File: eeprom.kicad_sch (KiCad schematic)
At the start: 4 parts, among them U2 AT24C04C_SOIC8

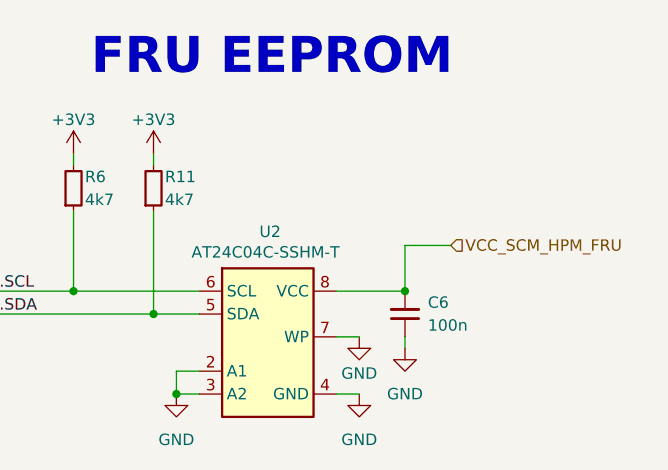
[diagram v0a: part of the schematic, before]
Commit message: [#92504] Add LTPI connector
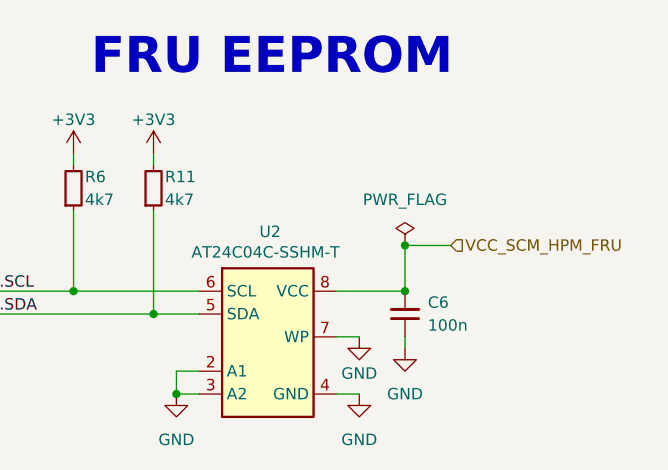
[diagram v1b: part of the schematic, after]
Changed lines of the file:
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@@
+	)
+	(junction
+		(at 100.33 45.72)
+		(diameter 0)
+		(color 0 0 0 0)
 	)
 	(junction
@@
 					(unit 1)
 				)
+			)
+		)
+	)
+	(symbol
+		(lib_name "PWR_FLAG_1")
+		(lib_id "antmicropower:PWR_FLAG")
+		(at 100.33 45.72 0)
+		(unit 1)
+		(exclude_from_sim no)
+		(in_bom yes)
+		(on_board yes)
+		(dnp no)
+		(fields_autoplaced yes)
+		(property "Reference" "#FLG04"
+			(at 100.33 43.815 0)
+			(effects
+				(font
+					(size 1.27 1.27)
+				)
+				(hide yes)
+			)
+		)
+		(property "Value" "PWR_FLAG"
+			(at 100.33 40.64 0)
+			(effects
+				(font
+					(size 1.27 1.27)
+				)
+			)
+		)
+		(property "Footprint" ""
+			(at 100.33 45.72 0)
+			(effects
+				(font
+					(size 1.27 1.27)
+				)
+				(hide yes)
+			)
+		)
+		(property "Datasheet" ""
+			(at 100.33 45.72 0)
+			(effects
+				(font
+					(size 1.27 1.27)
+				)
+				(hide yes)
+			)
+		)
+		(property "Description" ""
+			(at 100.33 48.26 0)
+			(effects
+				(font
+					(size 1.27 1.27)
+				)
+				(justify left bottom)
+				(hide yes)
+			)
+		)
+		(pin "1"
+		)
+		(instances
+			(project "bmc-breakout-board"
+				(path "/5d67ef28-5805-4f87-b722-2926dabf7f6e/2af4bc97-3599-45a7-a55a-50109ab85386"
+					(reference "#FLG04")
+					(unit 1)
+				)

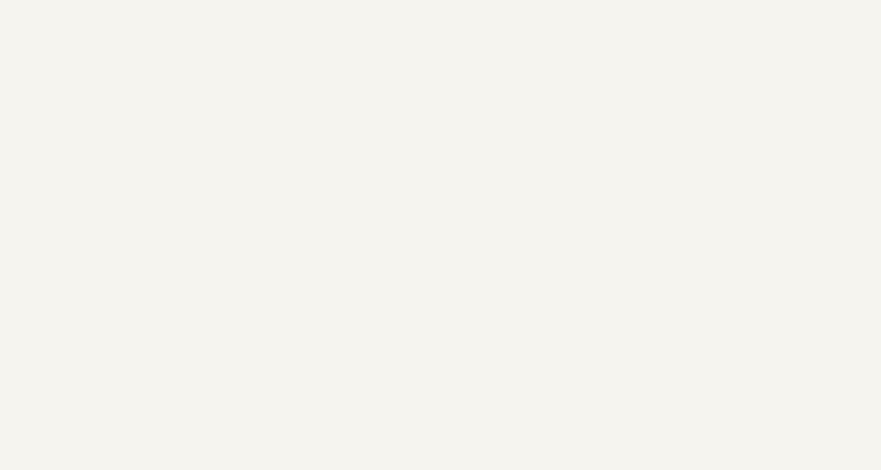
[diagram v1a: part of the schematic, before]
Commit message: [#92504] Add EEPROM power LED + TP
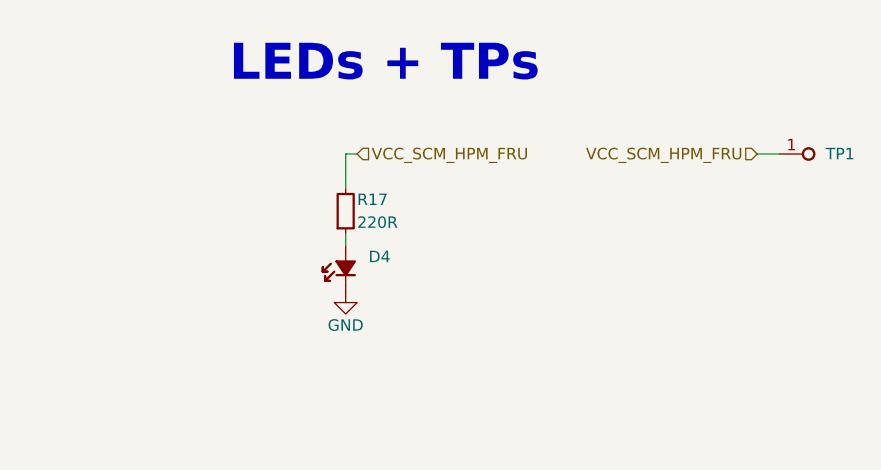
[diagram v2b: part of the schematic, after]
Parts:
- added D4: LED_G_0402_VLMTG1500-GS08, antmicro-footprints:LED_0402_1005Metric_G, symbol antmicroLEDIndicationDiscrete:LED_G_0402_VLMTG1500-GS08
- added R17: R_220R_0402, antmicro-footprints:R_0402_1005Metric, symbol antmicroResistors0402:R_220R_0402
- added TP1: TP_0.75mm_SMD, antmicro-footprints:TP_SMD_0.75mm, symbol antmicroTestPoints:TP_0.75mm_SMD
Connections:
- net GND: now also D4.1 (C)
- net VCC_SCM_HPM_FRU: now also R17.2, TP1.1
- new net: D4.2 (A), R17.1
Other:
- note added: "LEDs + TPs"

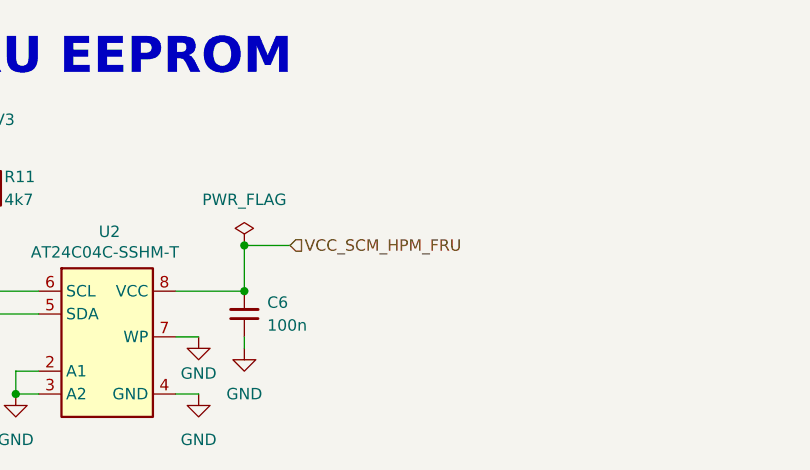
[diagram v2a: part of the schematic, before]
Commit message: [#92504] Add pull-up resistors for QWIIC
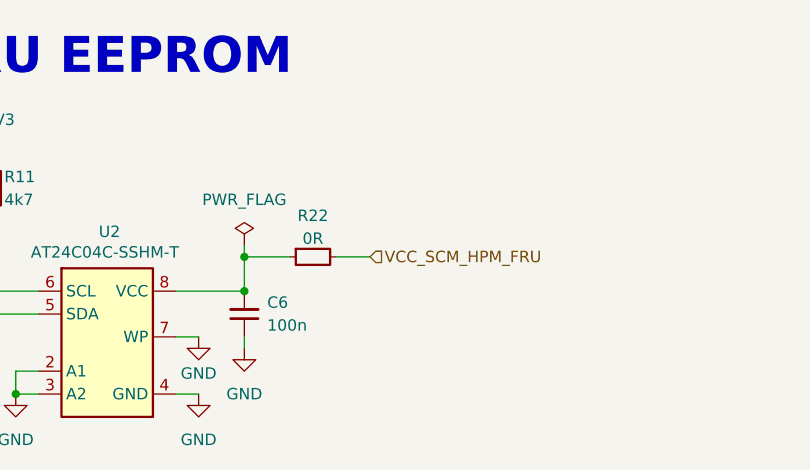
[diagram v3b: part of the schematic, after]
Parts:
- added R22: R_0R_0402, antmicro-footprints:R_0402_1005Metric, symbol antmicroResistors0402:R_0R_0402
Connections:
- net VCC_SCM_HPM_FRU: now also R22.2; no longer C6.2, U2.8 (VCC)
- new net: C6.2, R22.1, U2.8 (VCC)
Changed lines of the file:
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@@
-	)
-	(junction
-		(at 100.33 45.72)
-		(diameter 0)
-		(color 0 0 0 0)
 	)
 	(junction
@@
 	)
 	(junction
+		(at 100.33 46.99)
+		(diameter 0)
+		(color 0 0 0 0)
+	)
+	(junction
 		(at 72.39 53.34)
 		(diameter 0)
@@
 	(wire
 		(pts
+			(xy 110.49 46.99) (xy 114.3 46.99)
+		)
+		(stroke
+			(width 0)
+			(type default)
+		)
+	)
+	(wire
+		(pts
 			(xy 92.71 55.88) (xy 95.25 55.88)
 		)
@@
 	(wire
 		(pts
+			(xy 100.33 46.99) (xy 100.33 50.8)
+		)
+		(stroke
+			(width 0)
+			(type default)
+		)
+	)
+	(wire
+		(pts
 			(xy 267.97 35.56) (xy 270.51 35.56)
 		)
@@
 	(wire
 		(pts
+			(xy 100.33 46.99) (xy 105.41 46.99)
+		)
+		(stroke
+			(width 0)
+			(type default)
+		)
+	)
+	(wire
+		(pts
 			(xy 222.25 35.56) (xy 222.25 39.37)
 		)
@@
 	(wire
 		(pts
-			(xy 105.41 45.72) (xy 100.33 45.72)
-		)
-		(stroke
-			(width 0)
-			(type default)
-		)
-	)
-	(wire
-		(pts
-			(xy 100.33 45.72) (xy 100.33 50.8)
+			(xy 100.33 45.72) (xy 100.33 46.99)
 		)
 		(stroke
@@
 	(hierarchical_label "VCC_SCM_HPM_FRU"
 		(shape input)
-		(at 105.41 45.72 0)
+		(at 114.3 46.99 0)
 		(effects
 			(font
@@
 		)
 	)
+	(symbol
+		(lib_id "antmicroResistors0402:R_0R_0402")
+		(at 105.41 46.99 0)
+		(unit 1)
+		(exclude_from_sim no)
+		(in_bom yes)
+		(on_board yes)
+		(dnp no)
+		(property "Reference" "R22"
+			(at 107.95 42.418 0)
+			(effects
+				(font
+					(size 1.27 1.27)
+					(thickness 0.15)
+				)
+			)
+		)
+		(property "Value" "R_0R_0402"
+			(at 125.73 59.69 0)
+			(effects
+				(font
+					(size 1.27 1.27)
+					(thickness 0.15)
+				)
+				(justify left bottom)
+				(hide yes)
+			)
+		)
+		(property "Footprint" "antmicro-footprints:R_0402_1005Metric"
+			(at 125.73 62.23 0)
+			(effects
+				(font
+					(size 1.27 1.27)
+					(thickness 0.15)
+				)
+				(justify left bottom)
+				(hide yes)
+			)
+		)
+		(property "Datasheet" "https://industrial.panasonic.com/cdbs/www-data/pdf/RDA0000/AOA0000C301.pdf"
+			(at 125.73 64.77 0)
+			(effects
+				(font
+					(size 1.27 1.27)
+					(thickness 0.15)
+				)
+				(justify left bottom)
+				(hide yes)
+			)
+		)
+		(property "Description" "SMD Chip Resistor, Jumper, 0 ohm, 100 mW, 0402 [1005 Metric], Thick Film, General Purpose"
+			(at 125.73 80.01 0)
+			(effects
+				(font
+					(size 1.27 1.27)
+				)
+				(justify left bottom)
+				(hide yes)
+			)
+		)
+		(property "MPN" "ERJ2GE0R00X"
+			(at 125.73 67.31 0)
+			(effects
+				(font
+					(size 1.27 1.27)
+					(thickness 0.15)
+				)
+				(justify left bottom)
+				(hide yes)
+			)
+		)
+		(property "Manufacturer" "Panasonic"
+			(at 125.73 69.85 0)
+			(effects
+				(font
+					(size 1.27 1.27)
+					(thickness 0.15)
+				)
+				(justify left bottom)
+				(hide yes)
+			)
+		)
+		(property "License" "Apache-2.0"
+			(at 125.73 72.39 0)
+			(effects
+				(font
+					(size 1.27 1.27)
+					(thickness 0.15)
+				)
+				(justify left bottom)
+				(hide yes)
+			)
+		)
+		(property "Author" "Antmicro"
+			(at 125.73 74.93 0)
+			(effects
+				(font
+					(size 1.27 1.27)
+					(thickness 0.15)
+				)
+				(justify left bottom)
+				(hide yes)
+			)
+		)
+		(property "Val" "0R"
+			(at 107.95 44.958 0)
+			(effects
+				(font
+					(size 1.27 1.27)
+					(thickness 0.15)
+				)
+			)
+		)
+		(property "Tolerance" "~"
+			(at 125.73 57.15 0)
+			(effects
+				(font
+					(size 1.27 1.27)
+				)
+				(justify left bottom)
+				(hide yes)
+			)
+		)
+		(property "Current" "1A"
+			(at 125.73 77.47 0)
+			(effects
+				(font
+					(size 1.27 1.27)
+					(thickness 0.15)
+				)
+				(justify left bottom)
+				(hide yes)
+			)
+		)
+		(pin "2"
+		)
+		(pin "1"
+		)
+		(instances
+			(project "bmc-breakout-board"
+				(path "/5d67ef28-5805-4f87-b722-2926dabf7f6e/2af4bc97-3599-45a7-a55a-50109ab85386"
+					(reference "R22")
+					(unit 1)
+				)
+			)
+		)
+	)

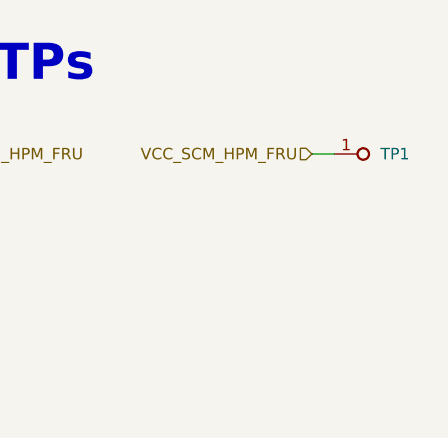
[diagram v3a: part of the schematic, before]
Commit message: [#92504] Clear Wire BUS errors
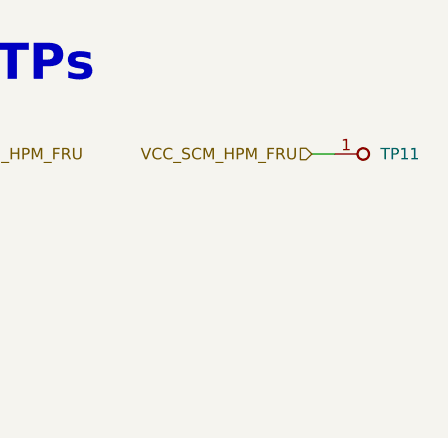
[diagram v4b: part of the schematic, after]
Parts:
- renumbered TP1 to TP11
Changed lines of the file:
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@@
 		(dnp no)
 		(fields_autoplaced yes)
-		(property "Reference" "TP1"
+		(property "Reference" "TP11"
 			(at 275.59 35.56 0)
 			(effects
@@
 			(project "bmc-breakout-board"
 				(path "/5d67ef28-5805-4f87-b722-2926dabf7f6e/2af4bc97-3599-45a7-a55a-50109ab85386"
-					(reference "TP1")
+					(reference "TP11")
 					(unit 1)
 				)

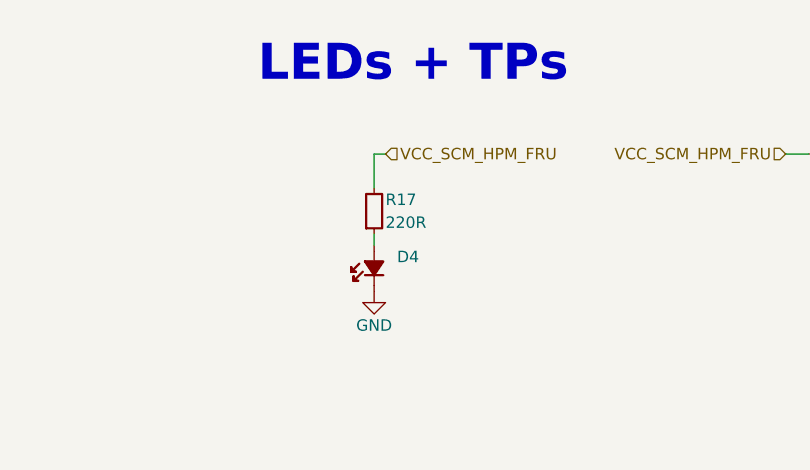
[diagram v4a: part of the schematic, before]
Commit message: [#92504] Clear ERC errors
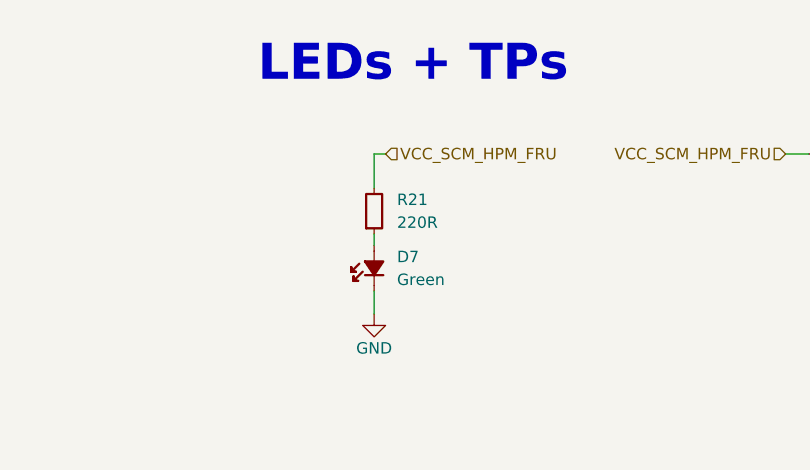
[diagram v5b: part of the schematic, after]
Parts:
- removed D4: LED_G_0402_VLMTG1500-GS08, antmicro-footprints:LED_0402_1005Metric_G, symbol antmicroLEDIndicationDiscrete:LED_G_0402_VLMTG1500-GS08
- removed R17: R_220R_0402, antmicro-footprints:R_0402_1005Metric, symbol antmicroResistors0402:R_220R_0402
- added D7: LED_G_0402_VLMTG1500-GS08, antmicro-footprints:LED_0402_1005Metric_G, symbol antmicroLEDIndicationDiscrete:LED_G_0402_VLMTG1500-GS08
- added R21: R_220R_0402, antmicro-footprints:R_0402_1005Metric, symbol antmicroResistors0402:R_220R_0402
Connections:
- net GND: now also D7.1 (C)
- net VCC_SCM_HPM_FRU: now also R21.2
- new net: D7.2 (A), R21.1

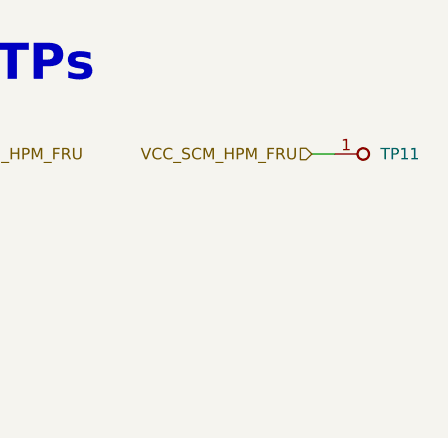
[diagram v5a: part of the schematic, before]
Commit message: [#92504] Change EEPROM TP value to 8
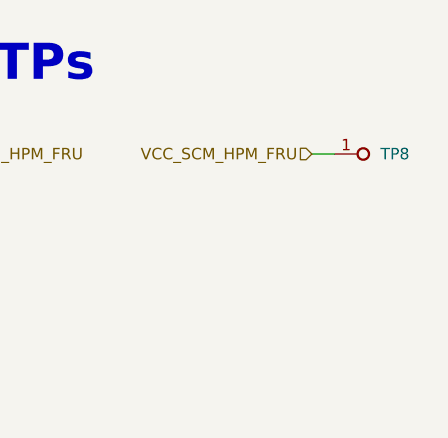
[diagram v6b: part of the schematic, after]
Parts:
- renumbered TP11 to TP8
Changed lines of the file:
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@@
 		(dnp no)
 		(fields_autoplaced yes)
-		(property "Reference" "TP11"
+		(property "Reference" "TP8"
 			(at 275.59 35.56 0)
 			(effects
@@
 			(project ""
 				(path "/5d67ef28-5805-4f87-b722-2926dabf7f6e/2af4bc97-3599-45a7-a55a-50109ab85386"
-					(reference "TP11")
+					(reference "TP8")
 					(unit 1)
 				)
